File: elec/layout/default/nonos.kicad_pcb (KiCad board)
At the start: 2 copper layers, 40 x 40 mm, 0 parts

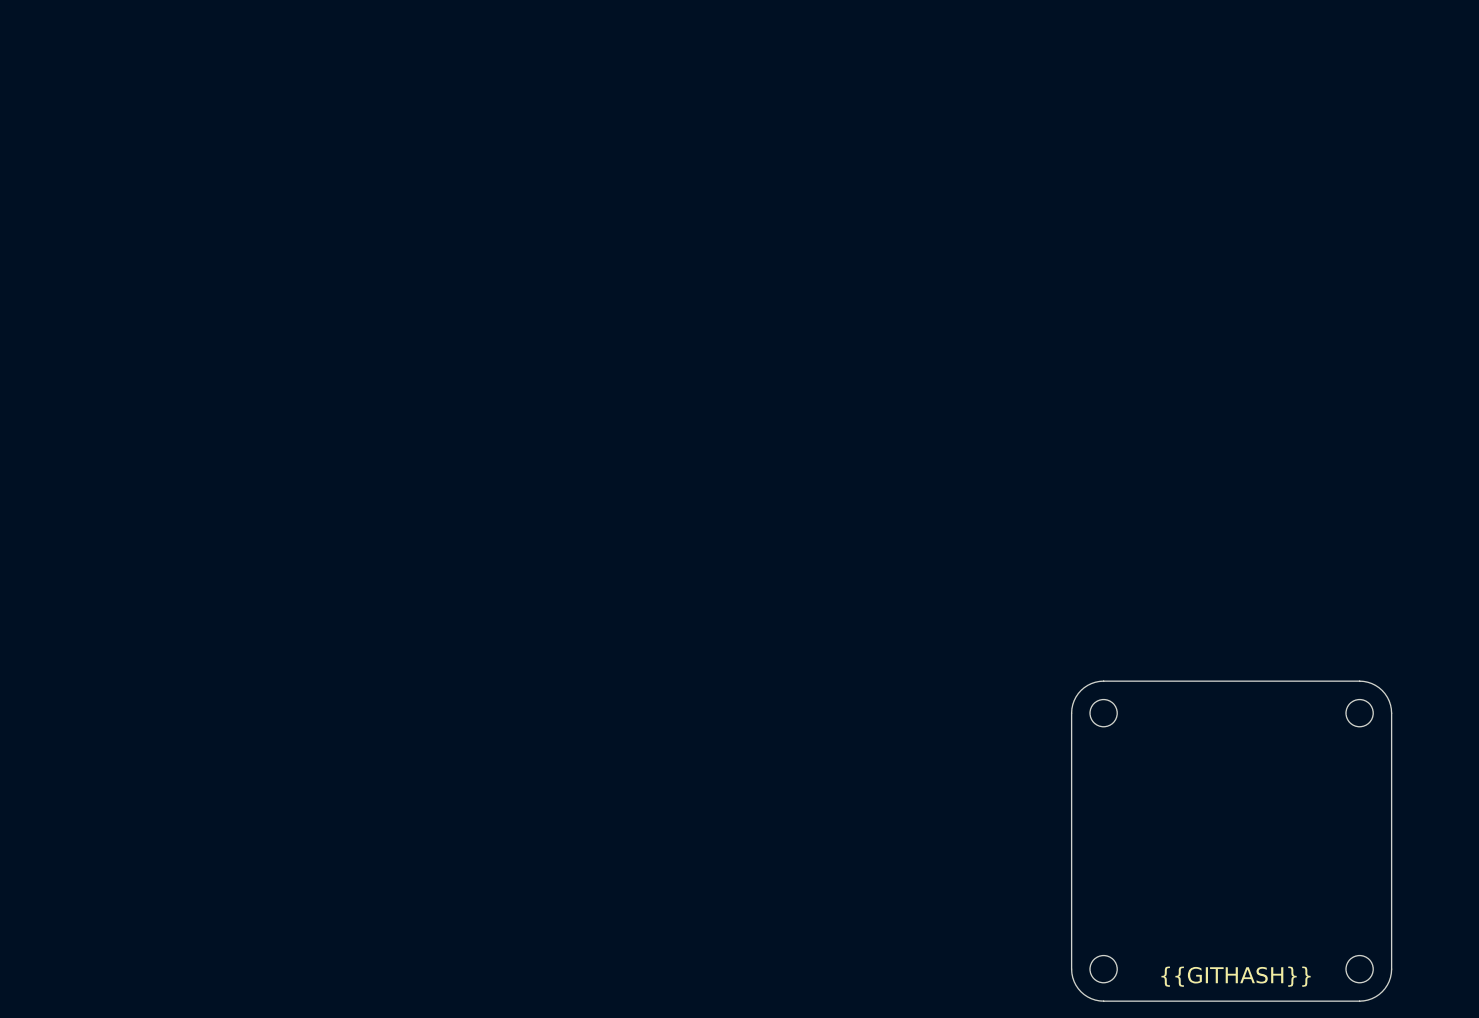
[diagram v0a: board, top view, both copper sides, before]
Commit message: Footprint path problems
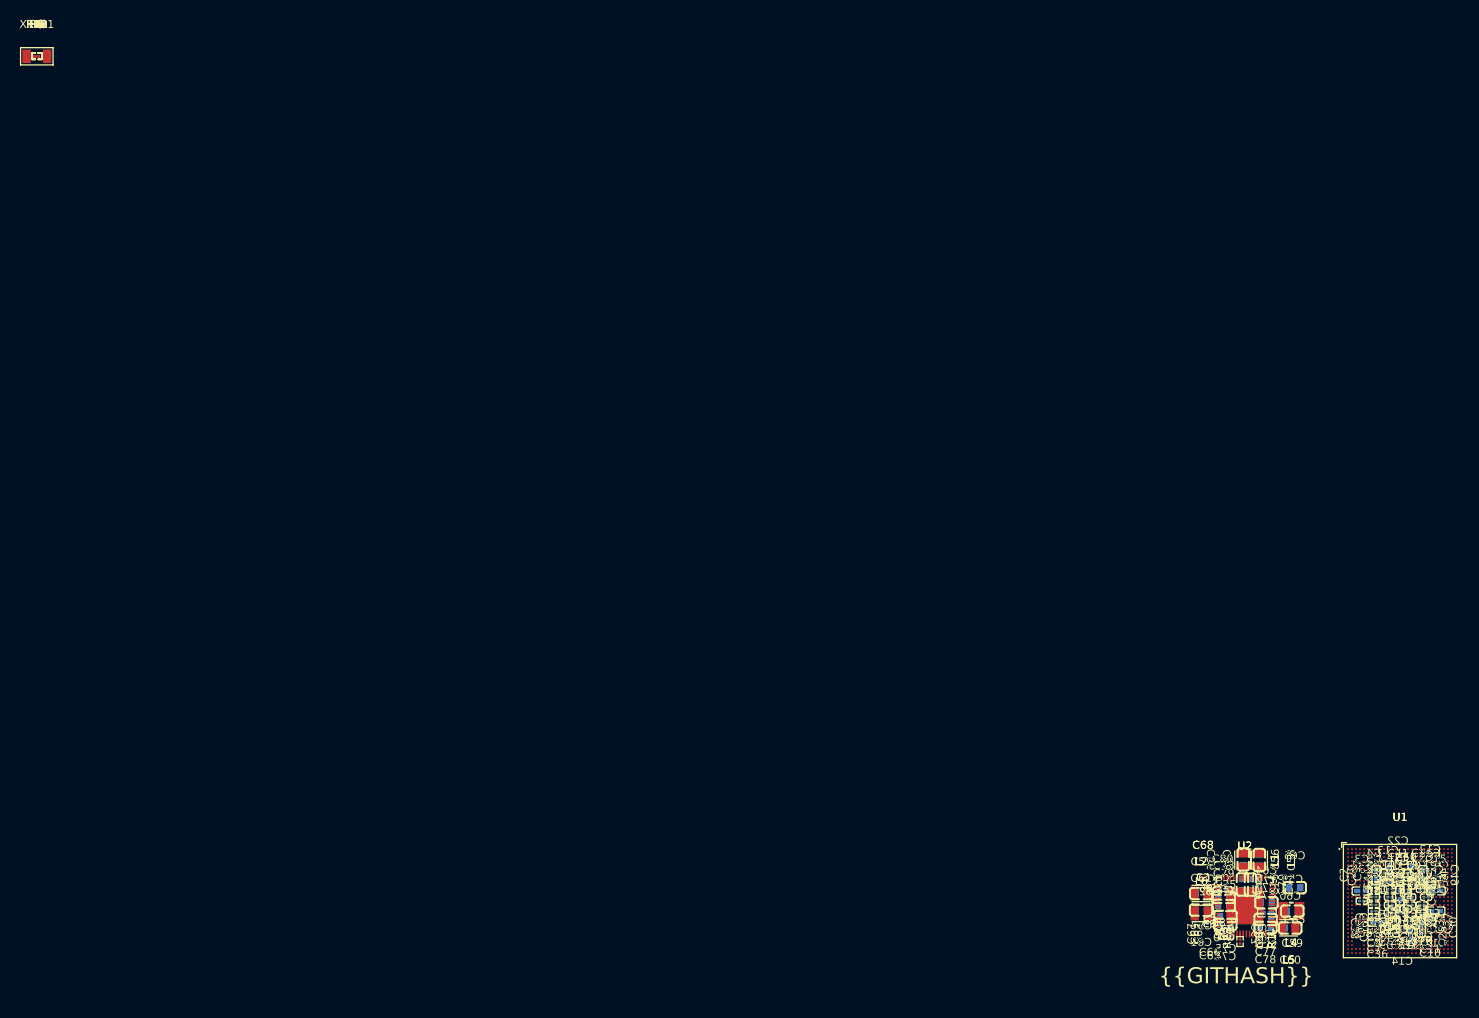
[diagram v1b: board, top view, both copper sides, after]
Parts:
- added C1: 2.2µF ±20% 6.3V X5R, lcsc:C0201, B.Cu at (170.9, 100.3)
- added C10: 220nF ±20% 6.3V X5R, lcsc:C0201, B.Cu at (174.2, 108.1)
- added C11: 220nF ±20% 6.3V X5R, lcsc:C0201, B.Cu at (174.2, 107.6)
- added C12: 1µF ±20% 6.3V X5R, lcsc:C0201, B.Cu at (174.1, 103.1)
- added C13: 220nF ±20% 6.3V X5R, lcsc:C0201, B.Cu at (168.9, 103.2)
- added C14: 1µF ±20% 6.3V X5R, lcsc:C0201, B.Cu at (170.7, 109.1)
- added C15: 10µF ±20% 6.3V X5R, lcsc:C0402, B.Cu at (174.9, 104.3)
- added C16: 220nF ±20% 6.3V X5R, lcsc:C0201, B.Cu at (169.9, 109.4)
- added C17: 10µF ±20% 6.3V X5R, lcsc:C0402, B.Cu at (174.8, 106.8)
- added C18: 220nF ±20% 6.3V X5R, lcsc:C0201, B.Cu at (173.2, 106.6)
- added C19: 220nF ±20% 6.3V X5R, lcsc:C0201, B.Cu at (173.7, 105.1)
- added C2: 10µF ±20% 6.3V X5R, lcsc:C0402, B.Cu at (167.4, 102.3)
- added C20: 220nF ±20% 6.3V X5R, lcsc:C0201, B.Cu at (173.1, 106.1)
- added C21: 220nF ±20% 6.3V X5R, lcsc:C0201, B.Cu at (173.2, 107.1)
- added C22: 220nF ±20% 6.3V X5R, lcsc:C0201, B.Cu at (170.1, 102.1)
- added C23: 220nF ±20% 6.3V X5R, lcsc:C0201, B.Cu at (173.1, 104.1)
- added C24: 220nF ±20% 6.3V X5R, lcsc:C0201, B.Cu at (169.4, 108.4)
- added C25: 4.7µF ±20% 10V X5R, lcsc:C0402, B.Cu at (171.7, 110.0)
- added C26: 220nF ±20% 6.3V X5R, lcsc:C0201, B.Cu at (173.1, 103.6)
- added C27: 220nF ±20% 6.3V X5R, lcsc:C0201, B.Cu at (172.4, 108.4)
- added C28: 220nF ±20% 6.3V X5R, lcsc:C0201, B.Cu at (168.8, 109.0)
- added C29: 220nF ±20% 6.3V X5R, lcsc:C0201, B.Cu at (168.4, 102.4)
- added C3: 10µF ±20% 6.3V X5R, lcsc:C0402, B.Cu at (165.6, 104.3)
- added C30: 10µF ±20% 6.3V X5R, lcsc:C0402, B.Cu at (173.0, 108.9)
- added C31: 1µF ±20% 6.3V X5R, lcsc:C0201, B.Cu at (170.6, 107.1)
- added C32: 1µF ±20% 6.3V X5R, lcsc:C0201, B.Cu at (171.4, 108.4)
- added C33: 1µF ±20% 6.3V X5R, lcsc:C0201, B.Cu at (171.1, 106.6)
- added C34: 1µF ±20% 6.3V X5R, lcsc:C0201, B.Cu at (169.6, 106.6)
- added C35: 1µF ±20% 6.3V X5R, lcsc:C0201, B.Cu at (169.9, 108.4)
- added C36: 10µF ±20% 6.3V X5R, lcsc:C0402, B.Cu at (167.6, 108.2)
- added C37: 10µF ±20% 6.3V X5R, lcsc:C0402, B.Cu at (169.1, 101.8)
- added C38: 1µF ±20% 6.3V X5R, lcsc:C0201, B.Cu at (165.6, 105.6)
- added C39: 1µF ±20% 6.3V X5R, lcsc:C0201, B.Cu at (169.1, 107.1)
- added C4: 1µF ±20% 6.3V X5R, lcsc:C0201, B.Cu at (167.1, 103.6)
- added C40: 1µF ±20% 6.3V X5R, lcsc:C0201, B.Cu at (169.2, 105.1)
- added C41: 1µF ±20% 6.3V X5R, lcsc:C0201, B.Cu at (170.1, 103.6)
- added C42: 1µF ±20% 6.3V X5R, lcsc:C0201, B.Cu at (169.1, 104.1)
- added C43: 1µF ±20% 6.3V X5R, lcsc:C0201, B.Cu at (169.2, 106.1)
- added C44: 220nF ±20% 6.3V X5R, lcsc:C0201, B.Cu at (170.4, 102.9)
- added C45: 2.2µF ±20% 6.3V X5R, lcsc:C0402, B.Cu at (171.9, 101.8)
- added C46: 220nF ±20% 6.3V X5R, lcsc:C0201, B.Cu at (171.3, 102.4)
- added C47: 220nF ±20% 6.3V X5R, lcsc:C0201, B.Cu at (174.1, 103.6)
- added C48: 10µF ±20% 6.3V X5R, lcsc:C0402, B.Cu at (170.4, 104.9)
- added C49: 4.7µF ±20% 10V X5R, lcsc:C0402, B.Cu at (173.3, 102.3)
- added C5: 1µF ±20% 6.3V X5R, lcsc:C0201, B.Cu at (167.1, 104.3)
- added C50: 1µF ±20% 6.3V X5R, lcsc:C0201, B.Cu at (171.1, 104.1)
- added C51: 1µF ±20% 6.3V X5R, lcsc:C0201, B.Cu at (171.1, 104.6)
- added C52: 1µF ±20% 6.3V X5R, lcsc:C0201, B.Cu at (171.7, 107.1)
- added C53: 1µF ±20% 6.3V X5R, lcsc:C0201, B.Cu at (171.7, 105.1)
- added C54: 1µF ±20% 6.3V X5R, lcsc:C0201, B.Cu at (171.9, 103.4)
- added C55: 220nF ±20% 6.3V X5R, lcsc:C0201, B.Cu at (171.6, 106.1)
- added C56: 22µF ±20% 6.3V X5R, lcsc:C0603, B.Cu at (150.8, 100.4)
- added C57: 22µF ±20% 6.3V X5R, lcsc:C0603, B.Cu at (145.6, 104.7)
- added C58: 22µF ±20% 6.3V X5R, lcsc:C0603, B.Cu at (152.8, 100.5)
- added C59: 22µF ±20% 6.3V X5R, lcsc:C0603, B.Cu at (156.9, 106.9)
- added C6: 1µF ±20% 6.3V X5R, lcsc:C0201, B.Cu at (167.1, 105.1)
- added C60: 22µF ±20% 6.3V X5R, lcsc:C0603, B.Cu at (156.7, 109.0)
- added C61: 22µF ±20% 6.3V X5R, lcsc:C0603, B.Cu at (145.5, 106.7)
- added C62: 1µF ±20% 6.3V X5R, lcsc:C0201, B.Cu at (146.6, 108.4)
- added C63: 1µF ±20% 6.3V X5R, lcsc:C0201, B.Cu at (149.2, 109.7)
- added C64: 4.7µF ±10% 16V X5R, lcsc:C0603, B.Cu at (153.7, 105.8)
- added C65: 4.7µF ±10% 16V X5R, lcsc:C0603, B.Cu at (157.2, 103.9)
- added C66: 1µF ±20% 6.3V X5R, lcsc:C0201, B.Cu at (146.6, 108.0)
- added C67: 1µF ±20% 6.3V X5R, lcsc:C0201, B.Cu at (148.3, 109.7)
- added C68: 1µF ±20% 6.3V X5R, lcsc:C0201, F.Cu at (145.8, 102.6)
- added C69: 1µF ±20% 6.3V X5R, lcsc:C0201, B.Cu at (148.8, 109.7)
- added C7: 1µF ±20% 6.3V X5R, lcsc:C0201, B.Cu at (167.1, 107.6)
- added C70: 10µF ±10% 10V X5R, lcsc:C0603, B.Cu at (151.7, 103.5)
- added C71: 2.2µF ±20% 10V X5R, lcsc:C0402, B.Cu at (152.5, 103.4)
- added C72: 2.2µF ±20% 10V X5R, lcsc:C0402, B.Cu at (153.8, 107.1)
- added C73: 10µF ±10% 10V X5R, lcsc:C0603, B.Cu at (148.4, 105.1)
- added C74: 10µF ±10% 10V X5R, lcsc:C0603, B.Cu at (148.6, 108.5)
- added C75: 10µF ±10% 10V X5R, lcsc:C0603, B.Cu at (148.6, 107.5)
- added C76: 10µF ±10% 10V X5R, lcsc:C0603, B.Cu at (150.7, 103.5)
- added C77: 10µF ±10% 10V X5R, lcsc:C0603, B.Cu at (153.6, 107.9)
- added C78: 10µF ±10% 10V X5R, lcsc:C0603, B.Cu at (153.6, 108.9)
- added C79: 10µF ±10% 10V X5R, lcsc:C0603, B.Cu at (148.4, 106.2)
- added C8: 1µF ±20% 6.3V X5R, lcsc:C0201, B.Cu at (167.1, 106.1)
- added C80: 2.2µF ±20% 10V X5R, lcsc:C0402, B.Cu at (148.2, 104.3)
- added C9: 1µF ±20% 6.3V X5R, lcsc:C0201, B.Cu at (167.1, 106.8)
- added L1: 470nH ±20% 3A - infA, lcsc:IND-SMD_L2.0-W1.6, F.Cu at (150.8, 100.5)
- added L2: 470nH ±20% 3A - infA, lcsc:IND-SMD_L2.0-W1.6, F.Cu at (145.5, 104.7)
- added L3: 470nH ±20% 3A - infA, lcsc:IND-SMD_L2.0-W1.6, F.Cu at (152.8, 100.5)
- added L4: 1µH ±20% 3A - infA, lcsc:IND-SMD_L2.5-W2.0-1, F.Cu at (156.8, 106.8)
- added L5: 470nH ±20% 3A - infA, lcsc:IND-SMD_L2.0-W1.6, F.Cu at (156.5, 108.9)
- added L6: 470nH ±20% 3A - infA, lcsc:IND-SMD_L2.0-W1.6, F.Cu at (145.6, 107.1)
- added R1: 4.87kΩ ±1% 50mW, lcsc:R0201, F.Cu at (150.4, 110.7)
- added R10, R11, R9: 100kΩ ±1% 50mW, lcsc:R0201, F.Cu at (0.00, 0.00)
- added R12: 10kΩ ±1% 50mW, lcsc:R0201, F.Cu at (0.00, 0.00)
- added R13: 1.5Ω ±5% 50mW, lcsc:R0201, F.Cu at (0.00, 0.00)
- added R2: 4.87kΩ ±1% 50mW, lcsc:R0201, F.Cu at (152.8, 110.7)
- added R3, R4, R5, R6, R7, R8: 4.87kΩ ±1% 50mW, lcsc:R0201, F.Cu at (0.00, 0.00)
- added U1: _NXP_Semicon_MIMX8MM6CVTKZAA, lcsc:BGA-486_L14.0-W14.0-P0.50-TL_NXP_MIMX8MMXDVTLZXA, F.Cu at (170.4, 105.6)
- added U2: _PCA9450AAHNY, lcsc:HVQFN-56_L7.0-W7.0-P0.40-BL-EP4.6, F.Cu at (151.0, 106.2)
- added XTAL1: Crystal_Oscillator, lcsc:OSC-SMD_L3.2-W1.5, F.Cu at (0.00, 0.00)
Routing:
- net *6468.PMIC-net-3: track 0.00 -> 1.81 mm
- net *6468.PMIC-net-10: track 0.00 -> 1.79 mm
- net (no net): track 0.00 -> 1.45 mm, vias 0 -> 1
- net GND: track 0.00 -> 0.48 mm, vias 0 -> 35
- net VDD_3V3: track 0.00 -> 0.46 mm, vias 0 -> 4
- net VDD_SOC_0V8: track 0.00 -> 0.10 mm, vias 0 -> 6
- net VDD_SNVS_0V8: track 0.00 -> 0.04 mm, vias 0 -> 1
- net NVCC_DRAM_1V1: track 0.00 -> 0.01 mm, vias 0 -> 14
- net jtag_trst_b: vias 0 -> 3
- net VDD_PHY_1V2: vias 0 -> 2
- net VDD_PHY_0V9: vias 0 -> 1
- net VDD_DRAM_0V9: vias 0 -> 7
- net VDD_ARM_0V9: vias 0 -> 5
- net VDD_1V8: vias 0 -> 9
- net NVCC_SD2: vias 0 -> 1
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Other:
- board outline removed

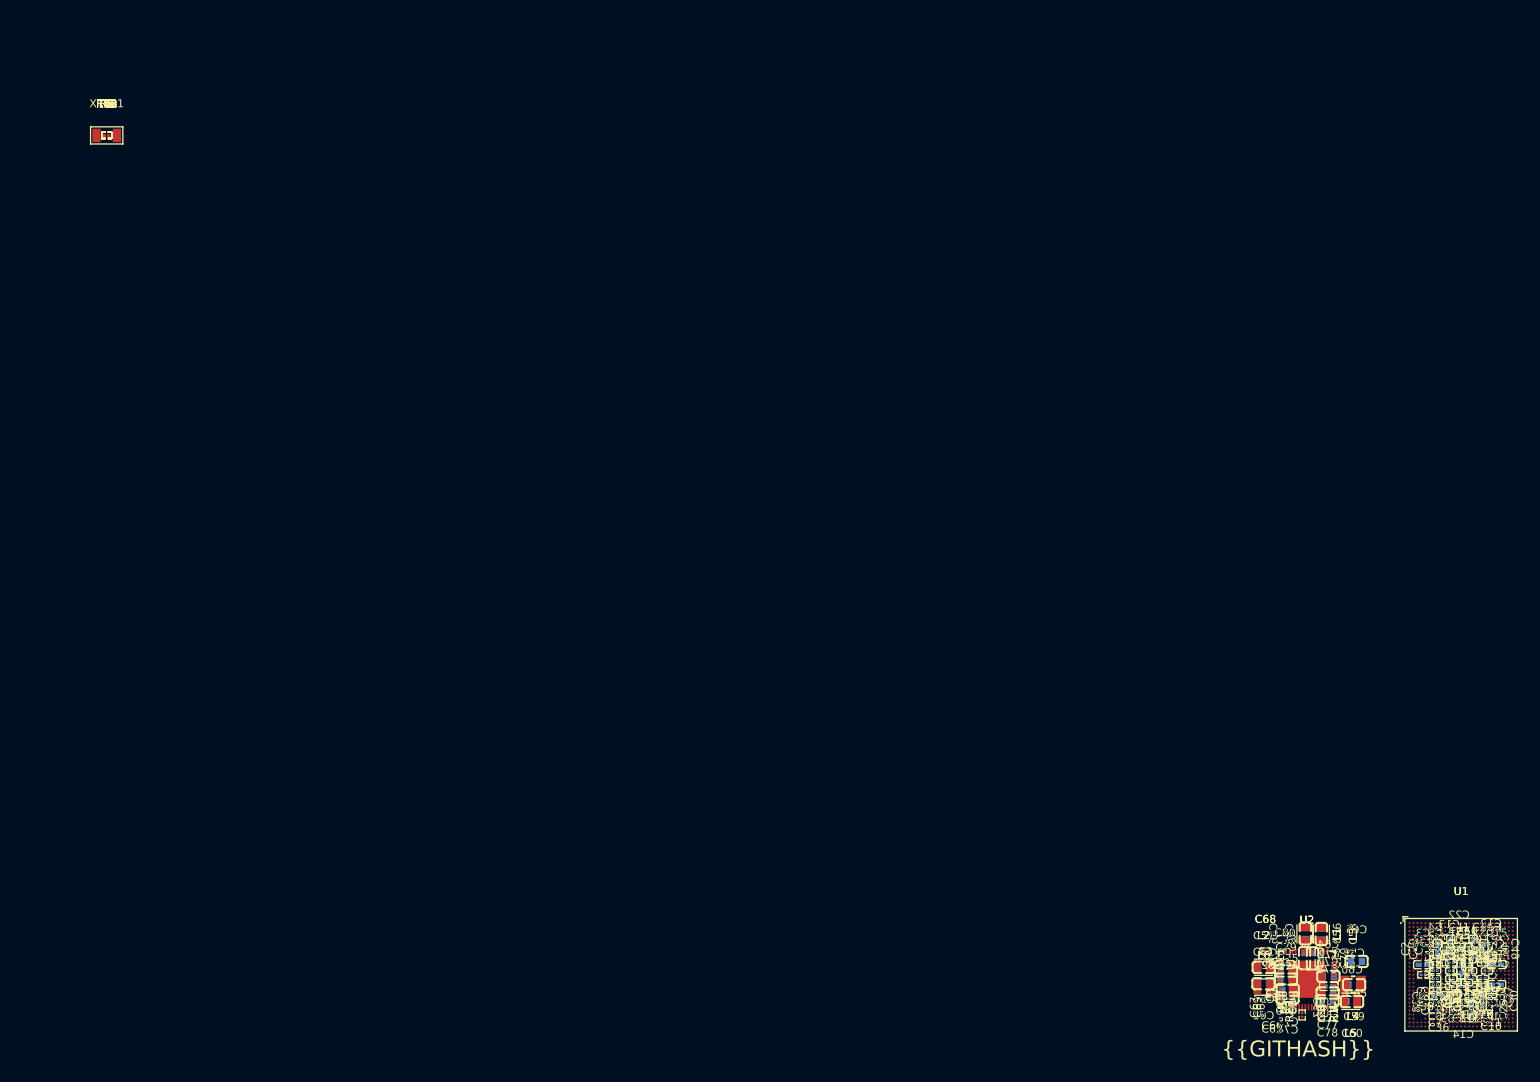
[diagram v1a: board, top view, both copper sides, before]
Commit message: add ethernet connector
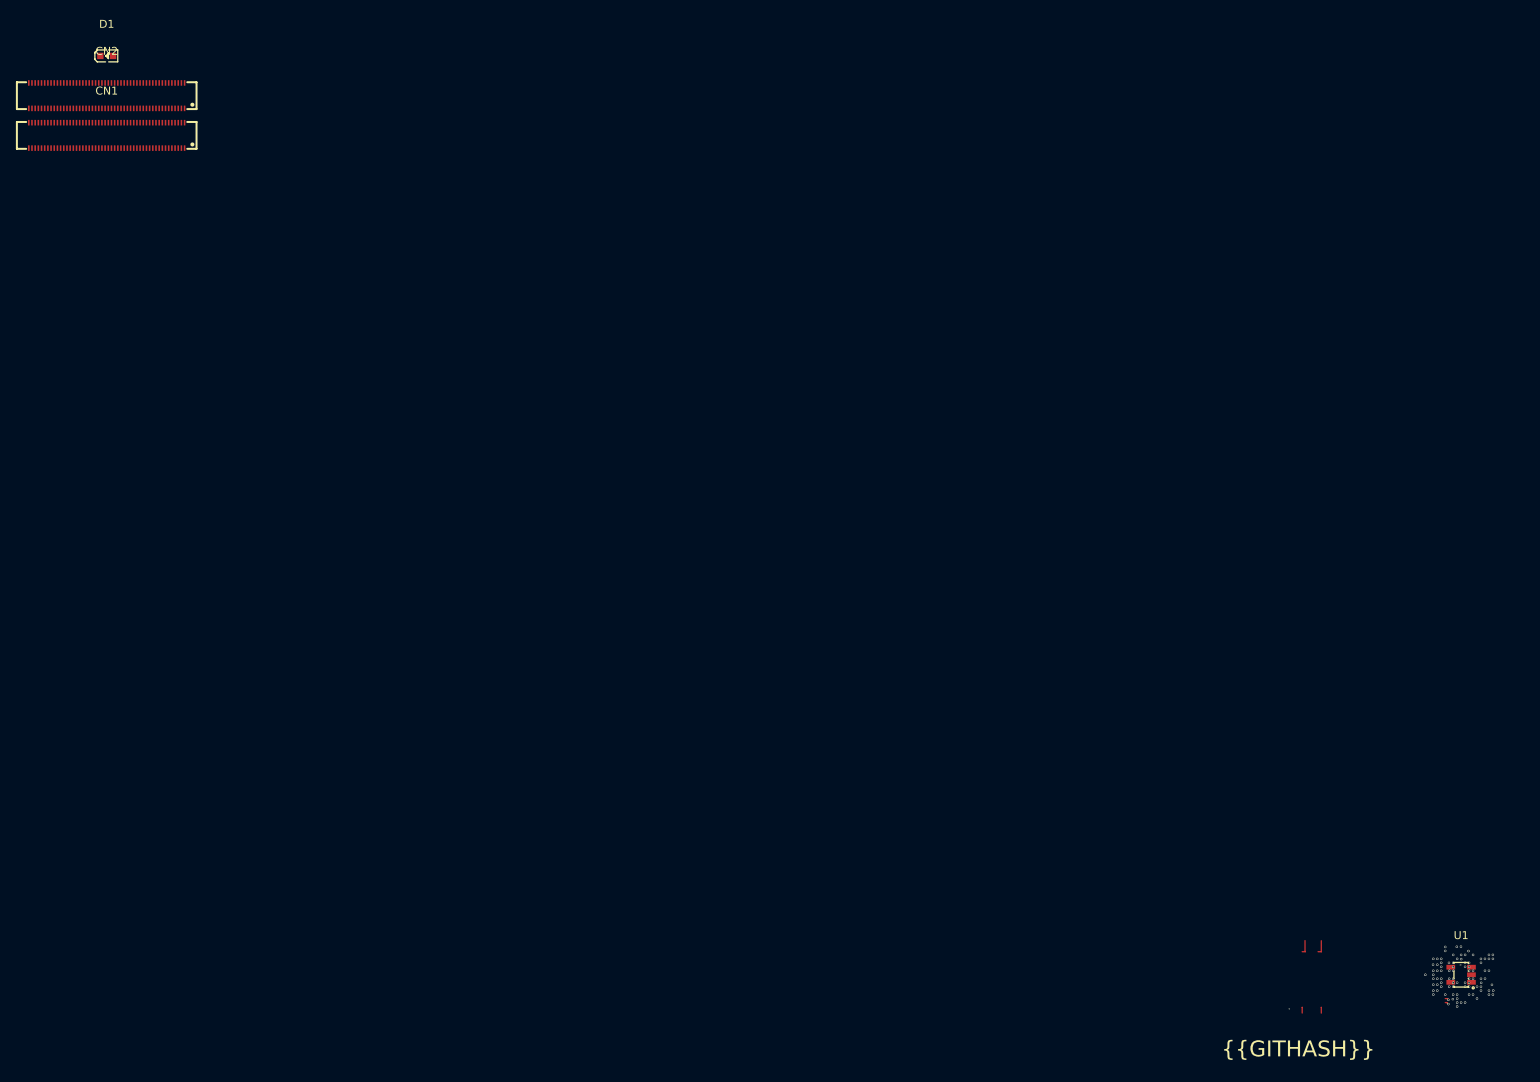
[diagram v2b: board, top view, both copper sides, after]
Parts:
- removed C1: 2.2µF ±20% 6.3V X5R, lcsc:C0201
- removed C10, C11, C13, C16, C18, C19, C20, C21, C22, C23, C24, C26, C27, C28, C29, C44, C46, C47, C55: 220nF ±20% 6.3V X5R, lcsc:C0201
- removed C12, C14, C31, C32, C33, C34, C35, C38, C39, C4, C40, C41, C42, C43, C5, C50, C51, C52, C53, C54, C6, C62, C63, C66, C67, C68, C69, C7, C8, C9: 1µF ±20% 6.3V X5R, lcsc:C0201
- removed C15, C17, C2, C3, C30, C36, C37, C48: 10µF ±20% 6.3V X5R, lcsc:C0402
- removed C25, C49: 4.7µF ±20% 10V X5R, lcsc:C0402
- removed C45: 2.2µF ±20% 6.3V X5R, lcsc:C0402
- removed C56, C57, C58, C59, C60, C61: 22µF ±20% 6.3V X5R, lcsc:C0603
- removed C64, C65: 4.7µF ±10% 16V X5R, lcsc:C0603
- removed C70, C73, C74, C75, C76, C77, C78, C79: 10µF ±10% 10V X5R, lcsc:C0603
- removed C71, C72, C80: 2.2µF ±20% 10V X5R, lcsc:C0402
- removed L1, L2, L3, L5, L6: 470nH ±20% 3A - infA, lcsc:IND-SMD_L2.0-W1.6
- removed L4: 1µH ±20% 3A - infA, lcsc:IND-SMD_L2.5-W2.0-1
- removed R1, R2, R3, R4, R5, R6, R7, R8: 4.87kΩ ±1% 50mW, lcsc:R0201
- removed R10, R11, R9: 100kΩ ±1% 50mW, lcsc:R0201
- removed R12: 10kΩ ±1% 50mW, lcsc:R0201
- removed R13: 1.5Ω ±5% 50mW, lcsc:R0201
- removed U2: _PCA9450AAHNY, lcsc:HVQFN-56_L7.0-W7.0-P0.40-BL-EP4.6
- removed XTAL1: Crystal_Oscillator, lcsc:OSC-SMD_L3.2-W1.5
- added CN1: HRSHirose_DF40C_100DS_0_4V51, lcsc:CONN-SMD_DF40C-100DS-0.4V-51, F.Cu at (0.00, 0.00)
- added CN2: HRSHirose_DF40C_100DS_0_4V51, lcsc:CONN-SMD_DF40C-100DS-0.4V-51, F.Cu at (0.00, -5.00)
- added D1: 2.7V, lcsc:LED0603-RD_WHITE, F.Cu at (0.00, -10.0)
- U1: value _NXP_Semicon_MIMX8MM6CVTKZAA -> _Texas_Instruments_SN74LVC1G07DBVR; footprint lcsc:BGA-486_L14.0-W14.0-P0.50-TL_NXP_MIMX8MMXDVTLZXA -> lcsc:SOT-23-5_L3.0-W1.7-P0.95-LS2.8-BR
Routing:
- net (no net): track 1.45 -> 5.67 mm, vias 1 -> 55
- net *6468.PMIC-net-3: track 1.81 -> 0.00 mm
- net *6468.PMIC-net-10: track 1.79 -> 0.00 mm
- net VDD_3V3: track 0.46 -> 0.00 mm, vias 4 -> 0
- net VDD_SOC_0V8: track 0.10 -> 0.00 mm, vias 6 -> 0
- net VDD_SNVS_0V8: track 0.04 -> 0.00 mm, vias 1 -> 0
- net NVCC_DRAM_1V1: track 0.01 -> 0.00 mm, vias 14 -> 0
- net jtag_trst_b: vias 3 -> 0
- net VDD_PHY_1V2: vias 2 -> 0
- net VDD_PHY_0V9: vias 1 -> 0
- net VDD_DRAM_0V9: vias 7 -> 0
- net VDD_ARM_0V9: vias 5 -> 0
- net VDD_1V8: vias 9 -> 0
- net NVCC_SD2: vias 1 -> 0
- net NVCC_ENET: vias 1 -> 0
